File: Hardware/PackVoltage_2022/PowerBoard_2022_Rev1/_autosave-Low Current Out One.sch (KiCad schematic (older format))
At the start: 32 parts

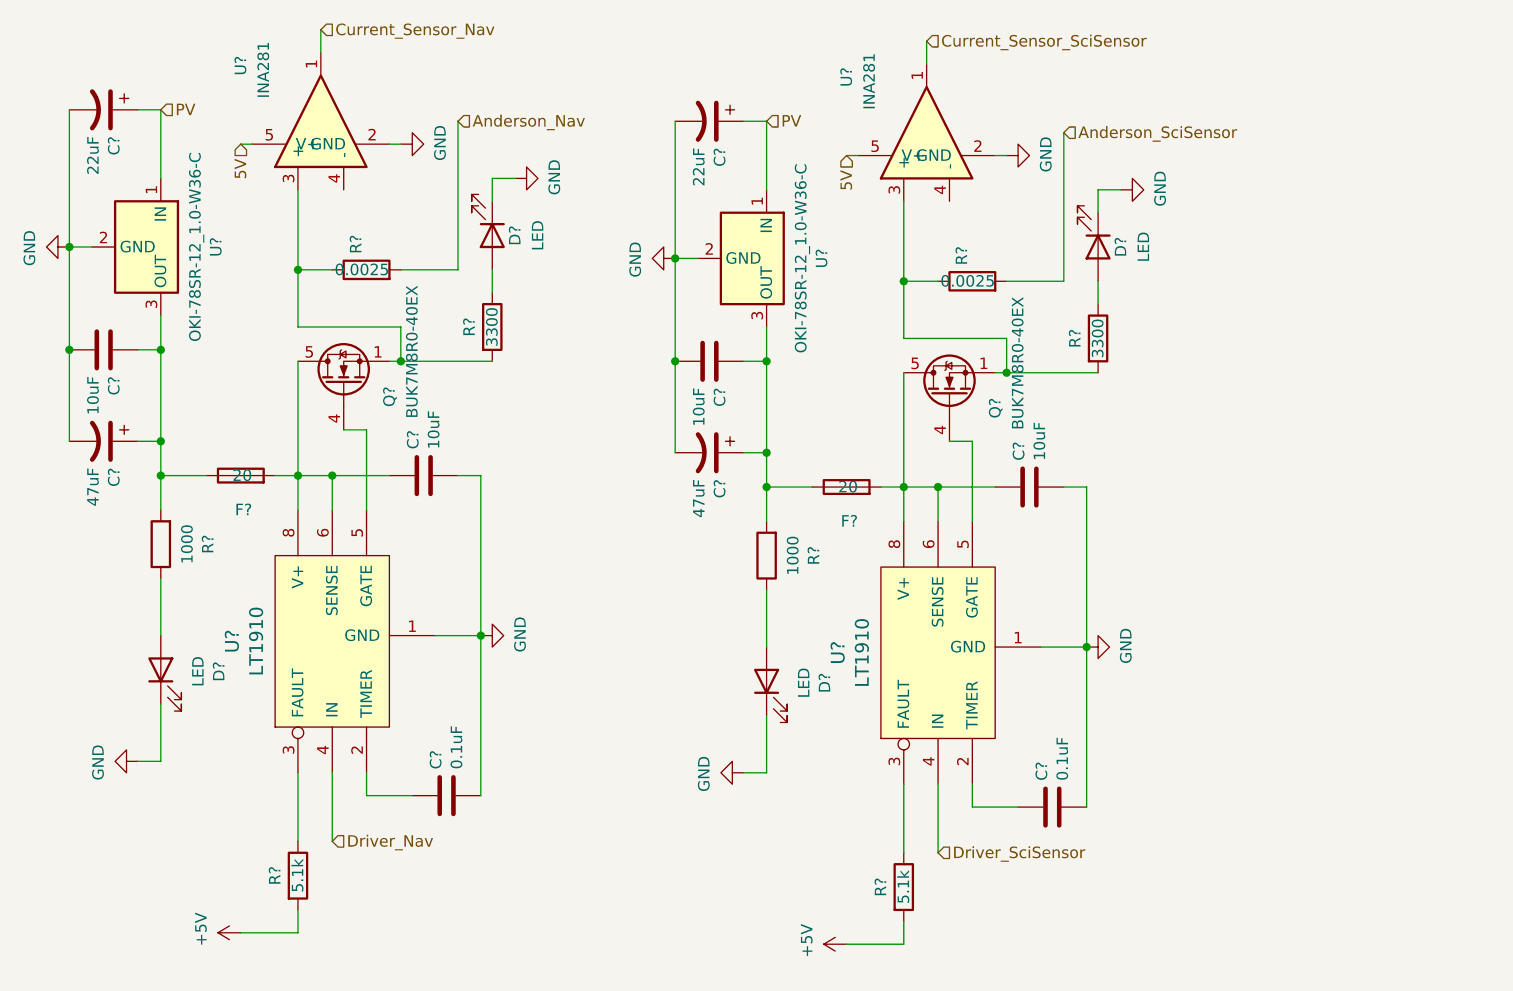
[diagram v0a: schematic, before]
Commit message: TIVA and fixed 12V
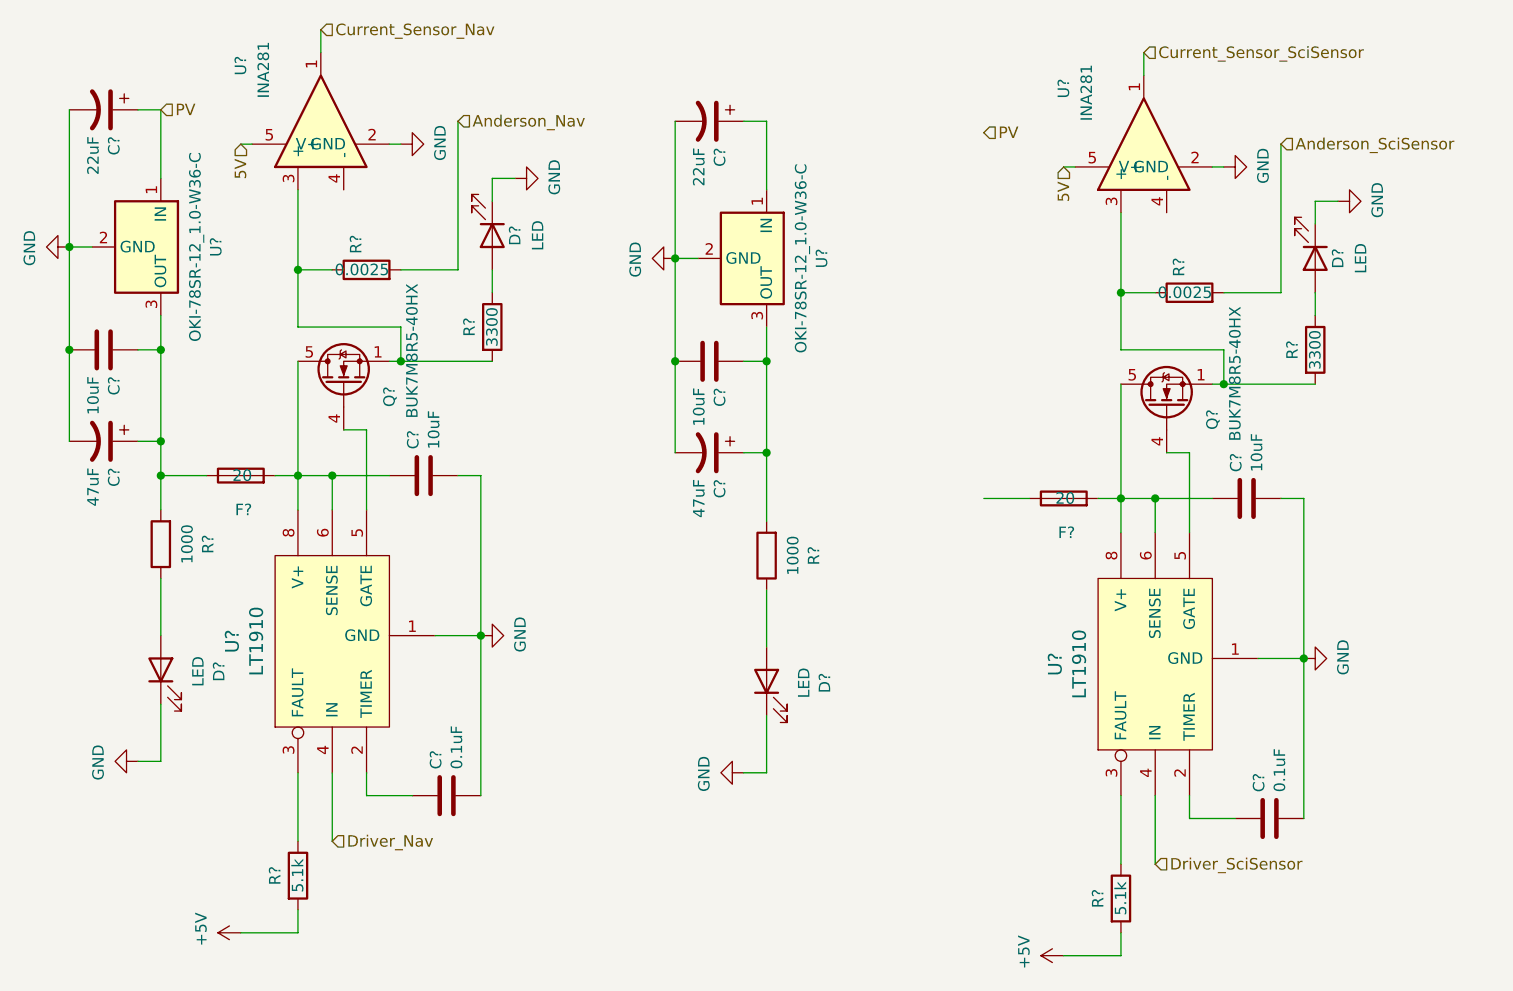
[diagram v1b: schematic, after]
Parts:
- Q? (x2): value BUK7M8R0-40EX -> BUK7M8R5-40HX
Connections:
- net PV: no longer C?.1, U?.1 (IN)
- net at C?.1, C?.1, R?.2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: no longer F?.1
- new net: C?.1, U?.1 (IN)
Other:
- moved on the sheet: C?, D?, F?, Q?, R?, U?
